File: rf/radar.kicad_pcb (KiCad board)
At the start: 4 copper layers, 52 x 68 mm, 136 parts, among them J101 Conn_01x02, J102 Conn_Coaxial, J103 Conn_01x04, J104 Conn_01x01, J105 Conn_01x01, J106 Conn_Coaxial, J107 Conn_01x02, J108 Conn_01x02, J801 Conn_01x02, T401 2450BL15B100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

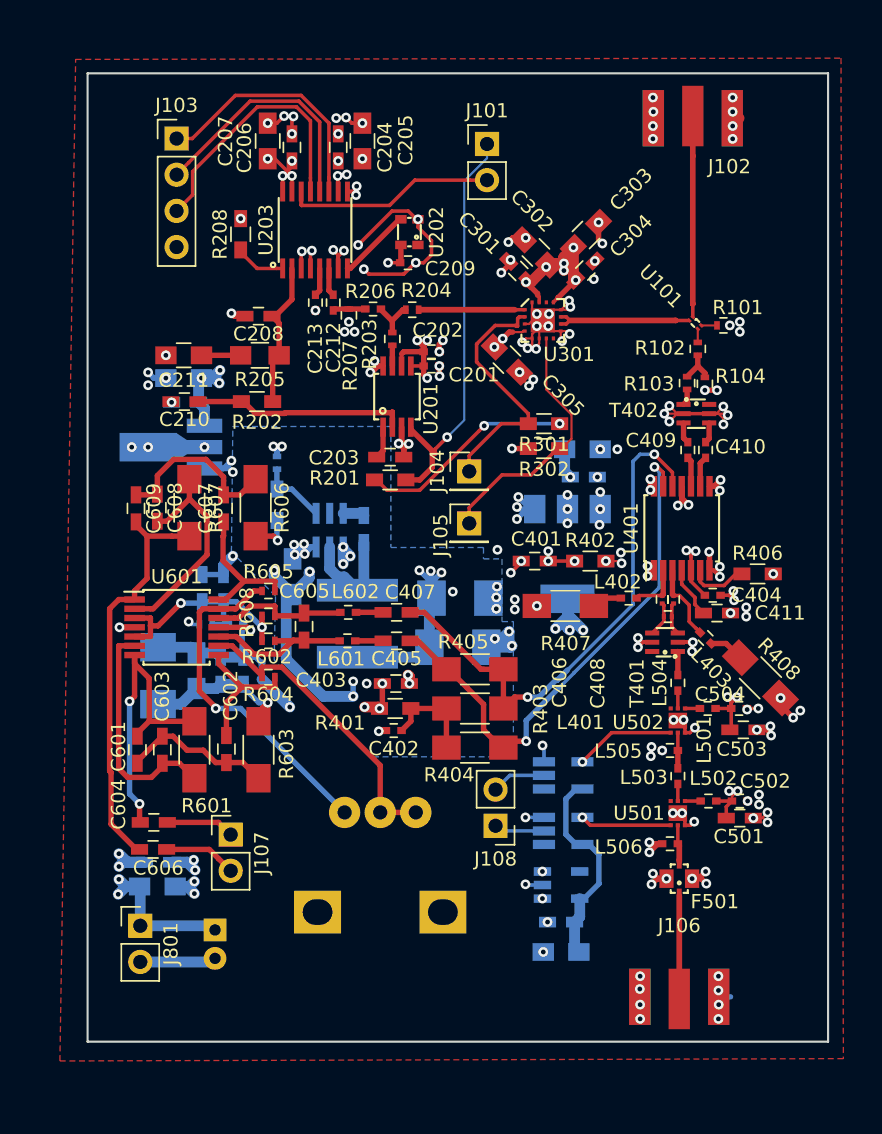
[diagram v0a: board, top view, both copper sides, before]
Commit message: Clean up PCB slightly
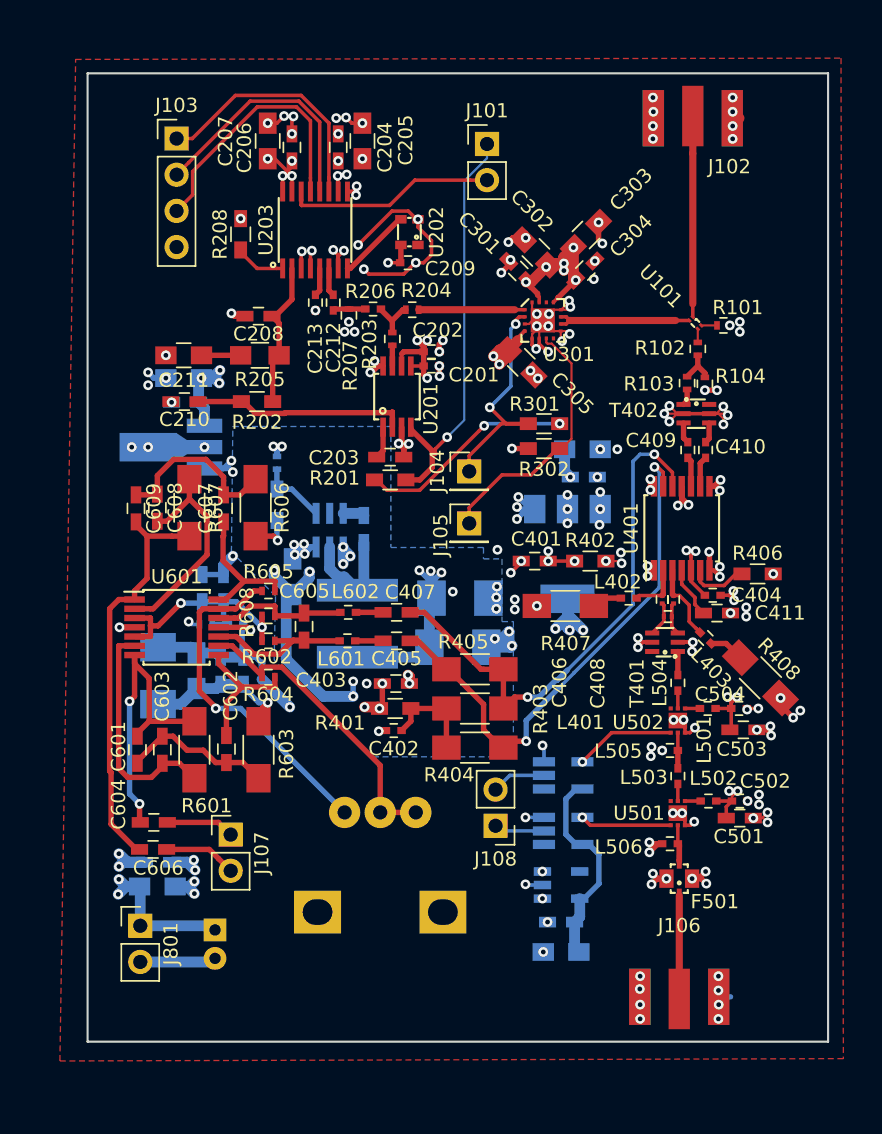
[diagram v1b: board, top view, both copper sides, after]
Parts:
- moved C305 1.02 mm to (130.5, 120.3)
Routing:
- net Net-(J102-Pad1): track 24.1 -> 14.1 mm
- net GND: track 831.8 -> 825.6 mm, vias 184 -> 182
- net /POWER_AMP/EN: track 17.8 -> 17.0 mm, vias 0 -> 2
- net /POWER_AMP/OUT: track 10.4 -> 9.83 mm

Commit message: Small fixes; update Gerber
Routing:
- net GND: track 825.6 -> 839.3 mm
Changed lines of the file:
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@@
     (thickness 1.6)
     (drawings 4)
-    (tracks 1740)
+    (tracks 1741)
     (zones 0)
     (modules 136)
@@
   )
   (setup
-    (last_trace_width 0.1524)
+    (last_trace_width 0.762)
     (user_trace_width 0.25)
     (user_trace_width 0.381)
@@
   (gr_line (start 152 100) (end 152 168) (layer Edge.Cuts) (width 0.15))
   (gr_line (start 100 100) (end 152 100) (layer Edge.Cuts) (width 0.15))
+  (segment (start 104.25 126.25) (end 104.25 124.75) (width 0.762) (layer B.Cu) (net 1))
+  (segment (start 104.25 124.75) (end 105.9 123.1) (width 0.762) (layer B.Cu) (net 1))
+  (segment (start 115.95 132.3) (end 115.95 130.9497) (width 0.762) (layer In2.Cu) (net 1))
+  (segment (start 115.95 130.9497) (end 115.95 130.45) (width 0.762) (layer In2.Cu) (net 1))
+  (segment (start 107.1877 130.9497) (end 115.95 130.9497) (width 0.762) (layer In2.Cu) (net 1))
+  (segment (start 104.25 126.25) (end 104.25 128.012) (width 0.762) (layer In2.Cu) (net 1))
+  (segment (start 104.25 128.012) (end 107.1877 130.9497) (width 0.762) (layer In2.Cu) (net 1))
+  (segment (start 104.25 126.25) (end 108.21 126.25) (width 0.762) (layer In2.Cu) (net 1))
+  (segment (start 103.1 126.25) (end 104.25 126.25) (width 0.762) (layer In2.Cu) (net 1))
   (segment (start 131.715 118.615) (end 131.715 119.0025) (width 0.25) (layer F.Cu) (net 1))
   (segment (start 128.4 129.7) (end 131 127.1) (width 0.762) (layer In1.Cu) (net 1))
@@
   (segment (start 117.95 133.262) (end 118.962 133.262) (width 0.762) (layer In2.Cu) (net 1))
   (segment (start 118.962 133.262) (end 119.35 132.874) (width 0.762) (layer In2.Cu) (net 1))
-  (segment (start 115.95 132.3) (end 115.95 130.45) (width 0.762) (layer In2.Cu) (net 1))
   (segment (start 116.912 133.262) (end 115.95 132.3) (width 0.762) (layer In2.Cu) (net 1))
   (segment (start 116.938 133.262) (end 116.912 133.262) (width 0.762) (layer In2.Cu) (net 1))
@@
   (segment (start 118.35 117.85) (end 118.05 118.15) (width 0.762) (layer In1.Cu) (net 1))
   (segment (start 115.75 112.45) (end 115.75 114.85) (width 0.762) (layer In1.Cu) (net 1))
-  (segment (start 108.21 126.25) (end 108.21 125.41) (width 0.762) (layer In1.Cu) (net 1))
-  (segment (start 108.21 125.41) (end 105.9 123.1) (width 0.762) (layer In1.Cu) (net 1))
-  (segment (start 103.1 126.25) (end 103.442899 125.907101) (width 0.762) (layer In1.Cu) (net 1))
-  (segment (start 103.442899 125.907101) (end 103.442899 125.557101) (width 0.762) (layer In1.Cu) (net 1))
-  (segment (start 103.442899 125.557101) (end 104.25 124.75) (width 0.762) (layer In1.Cu) (net 1))
-  (segment (start 104.25 126.25) (end 104.25 124.75) (width 0.762) (layer In1.Cu) (net 1))
-  (segment (start 104.25 124.75) (end 105.9 123.1) (width 0.762) (layer In1.Cu) (net 1))
   (segment (start 105.625 121.4) (end 106.275 120.75) (width 0.762) (layer In1.Cu) (net 1))
   (segment (start 106.275 120.75) (end 107.15 119.875) (width 0.762) (layer In1.Cu) (net 1))
@@
     (polygon
       (pts
-        (xy 121.3 124.8) (xy 121.3 129) (xy 121.3 133.3) (xy 127.8 133.3) (xy 127.8 134.1)
-        (xy 129.1 134.1) (xy 129.1 138.5) (xy 129.9 138.5) (xy 129.9 141.6) (xy 129.9 144.5)
-        (xy 129.9 148) (xy 119.9 148) (xy 113.1 141.2) (xy 113.2 136.7) (xy 110.1 133.6)
-        (xy 110.2 124.8)
+        (xy 121.3612 123.4567) (xy 121.3 133.3) (xy 127.8 133.3) (xy 127.8 134.1) (xy 129.1 134.1)
+        (xy 129.1 138.5) (xy 129.9 138.5) (xy 129.9 148) (xy 119.9 148) (xy 113.1 141.2)
+        (xy 113.2 136.7) (xy 110.1 133.6) (xy 110.15 129.2) (xy 101.5238 129.2352) (xy 101.6127 123.4186)
       )
     )
@@
         (xy 128.8 140.8) (xy 128.3 140.3) (xy 118 140.3) (xy 118 145) (xy 119 145)
         (xy 119 149) (xy 128 149) (xy 128 168) (xy 100 168) (xy 100 127.2)
-        (xy 128.3 127.2) (xy 128.3 126.7) (xy 100 126.7) (xy 100 100) (xy 152 100)
+        (xy 128.3 127.2) (xy 128.3 126.7) (xy 111.3028 126.7079) (xy 111.3028 125.1839) (xy 99.9998 125.1839)
+        (xy 100 100) (xy 152 100)
       )
     )

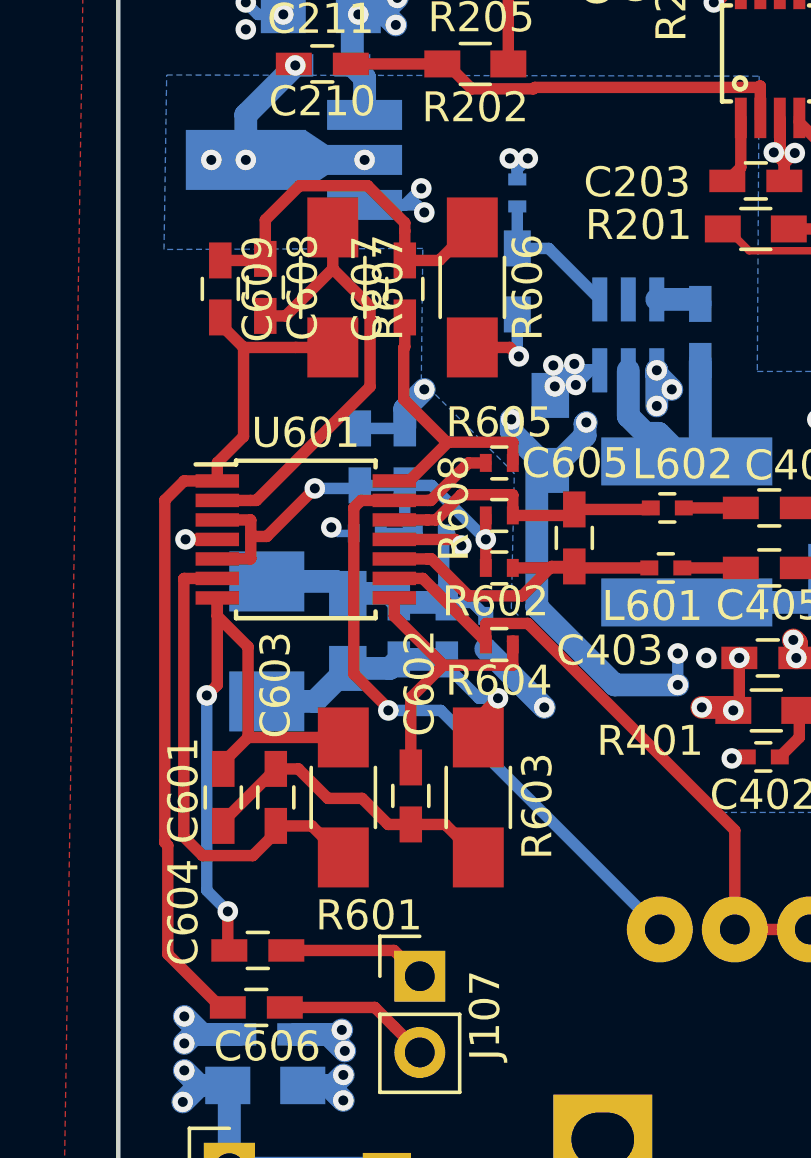
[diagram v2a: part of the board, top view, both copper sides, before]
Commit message: Convert high pass from MFB to Sallen-Key; forgot about low input impedance for high pass MFB
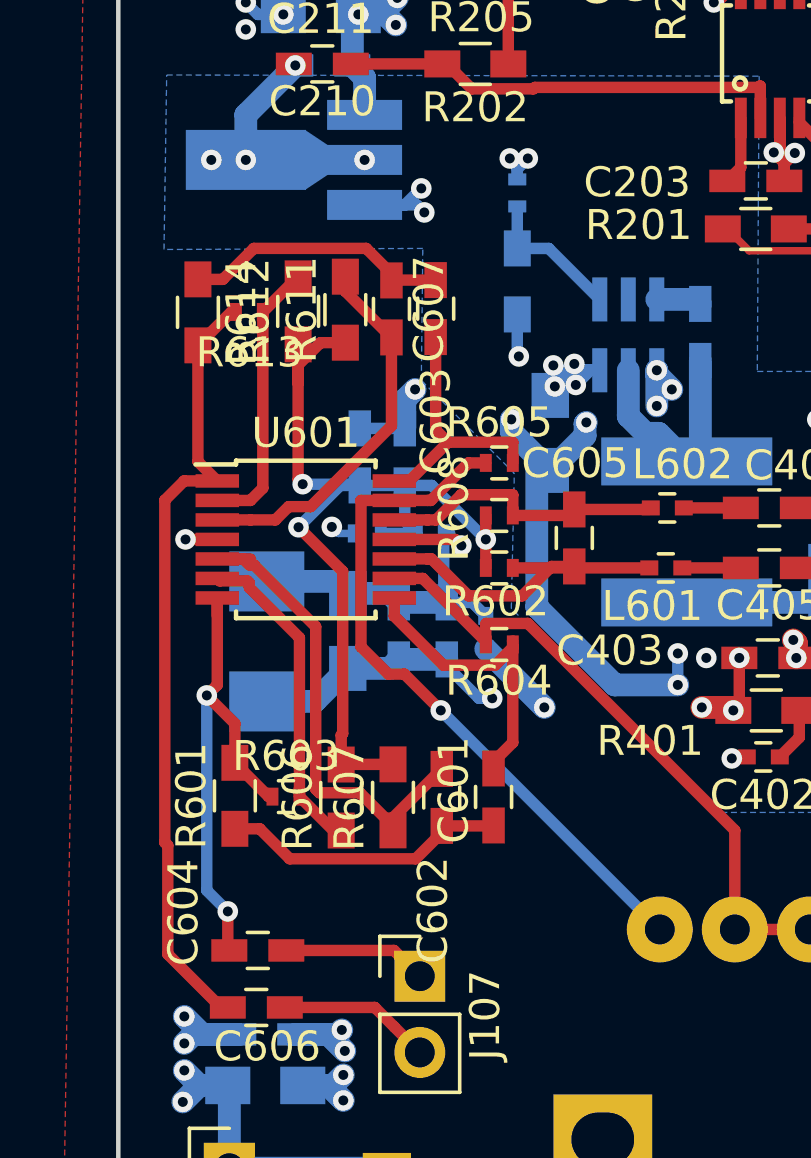
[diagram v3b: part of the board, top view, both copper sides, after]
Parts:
- removed C608: 8n5, Capacitors_SMD:C_0603_HandSoldering
- removed C609: 2n2, Capacitors_SMD:C_0603_HandSoldering
- added R611: 47k, Resistors_SMD:R_0603_HandSoldering, F.Cu at (107.6, 131.2)
- added R612: 47k, Resistors_SMD:R_0603_HandSoldering, F.Cu at (106.0, 131.3)
- added R613: 150k, Resistors_SMD:R_0402, F.Cu at (104.4, 131.3)
- added R614: 47k, Resistors_SMD:R_0603_HandSoldering, F.Cu at (102.7, 131.3)
- C601: value 2n2 -> 33p
- C602, C603, C607: value 8n5 -> 33p
- R601, R607: value 1k -> 47k; footprint Resistors_SMD:R_1206_HandSoldering -> Resistors_SMD:R_0603_HandSoldering
- R603: value 165 -> 150k; footprint Resistors_SMD:R_1206_HandSoldering -> Resistors_SMD:R_0402
- R606: value 165 -> 47k; footprint Resistors_SMD:R_1206_HandSoldering -> Resistors_SMD:R_0603_HandSoldering
- moved R606 17.6 mm to (107.4, 147.5), turned to 90 degrees
- moved C603 17.1 mm to (110.6, 131.2), turned to 90 degrees
- moved R607 17.1 mm to (109.2, 147.5), turned to 90 degrees
- moved C601 9.01 mm to (112.5, 147.5)
- moved R603 6.41 mm to (105.6, 147.5), turned to 0 degrees
- moved R601 3.61 mm to (103.9, 147.4), turned to 90 degrees
- moved C602 1.03 mm to (110.8, 147.5), turned to 90 degrees
- moved C607 0.80 mm to (109.1, 131.2), turned to 270 degrees
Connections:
- C602 pad 1: Net-(C602-Pad1) -> Net-(C601-Pad2)
- C602 pad 2: Net-(C601-Pad2) -> Net-(C602-Pad2)
- C603 pad 1: Net-(C601-Pad2) -> Net-(C603-Pad1)
- C604 pad 1: Net-(C601-Pad1) -> Net-(C604-Pad1)
- C607 pad 1: Net-(C607-Pad1) -> Net-(C603-Pad2)
- R601 pad 1: Net-(C601-Pad1) -> Net-(C601-Pad2)
- R601 pad 2: Net-(C603-Pad2) -> Net-(C604-Pad1)
- R603 pad 1: Net-(C601-Pad2) -> Net-(C604-Pad1)
- R603 pad 2: GND -> Net-(R603-Pad2)
- R604 pad 1: Net-(C602-Pad1) -> Net-(C601-Pad1)
- R605 pad 2: Net-(C607-Pad1) -> Net-(C603-Pad1)
- R606 pad 1: Net-(C607-Pad2) -> Net-(R603-Pad2)
- R606 pad 2: GND -> +6V
- R607 pad 1: Net-(C608-Pad2) -> Net-(C602-Pad2)
- R607 pad 2: Net-(C606-Pad1) -> +6V
- U601 pad 14: Net-(C607-Pad1) -> Net-(C603-Pad1)
- U601 pad 2: Net-(C608-Pad2) -> Net-(R612-Pad2)
- U601 pad 3: +6V -> Net-(C607-Pad2)
- U601 pad 5: +6V -> Net-(C602-Pad2)
- U601 pad 6: Net-(C603-Pad2) -> Net-(R603-Pad2)
- U601 pad 7: Net-(C601-Pad1) -> Net-(C604-Pad1)
- U601 pad 8: Net-(C602-Pad1) -> Net-(C601-Pad1)
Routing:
- net Net-(C604-Pad1): track 0.00 -> 17.2 mm, vias 0 -> 2
- net Net-(C602-Pad2): track 0.00 -> 16.0 mm
- net Net-(C608-Pad2): track 15.4 -> 0.00 mm
- net +6V: track 17.5 -> 31.8 mm, vias 2 -> 3
- net Net-(C601-Pad1): track 21.8 -> 9.99 mm, vias 2 -> 0
- net Net-(R603-Pad2): track 0.00 -> 10.8 mm
- net Net-(C607-Pad1): track 9.98 -> 0.00 mm
- net Net-(C602-Pad1): track 9.79 -> 0.00 mm
- net Net-(R612-Pad2): track 0.00 -> 9.20 mm
- net Net-(C603-Pad1): track 0.00 -> 8.89 mm
- net Net-(C603-Pad2): track 16.3 -> 8.93 mm
- net GND: track 839.3 -> 835.9 mm
- net Net-(C606-Pad1): track 29.0 -> 26.4 mm
- net Net-(C601-Pad2): track 10.6 -> 9.63 mm
- net Net-(R605-Pad1): track 24.3 -> 23.4 mm

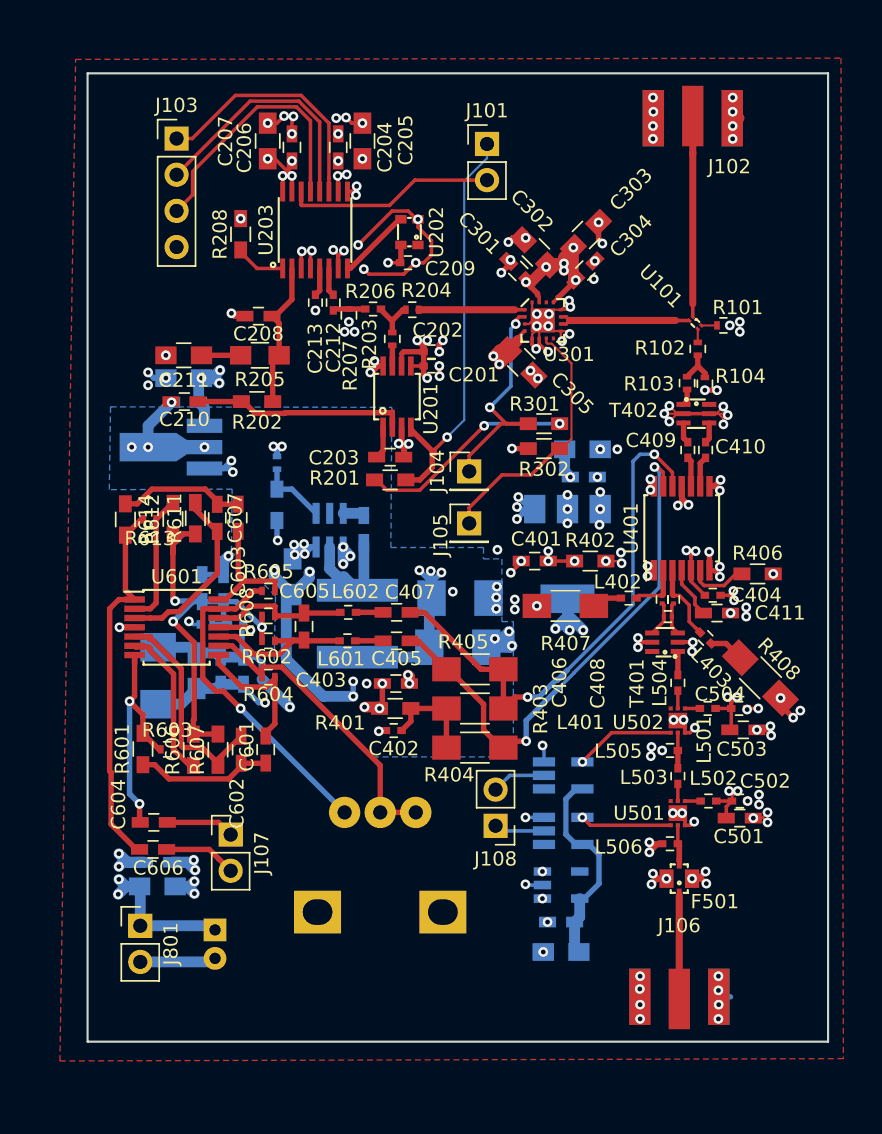
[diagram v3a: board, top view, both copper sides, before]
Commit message: Massage vias to improve planes and swap out connectors to get more ground lines
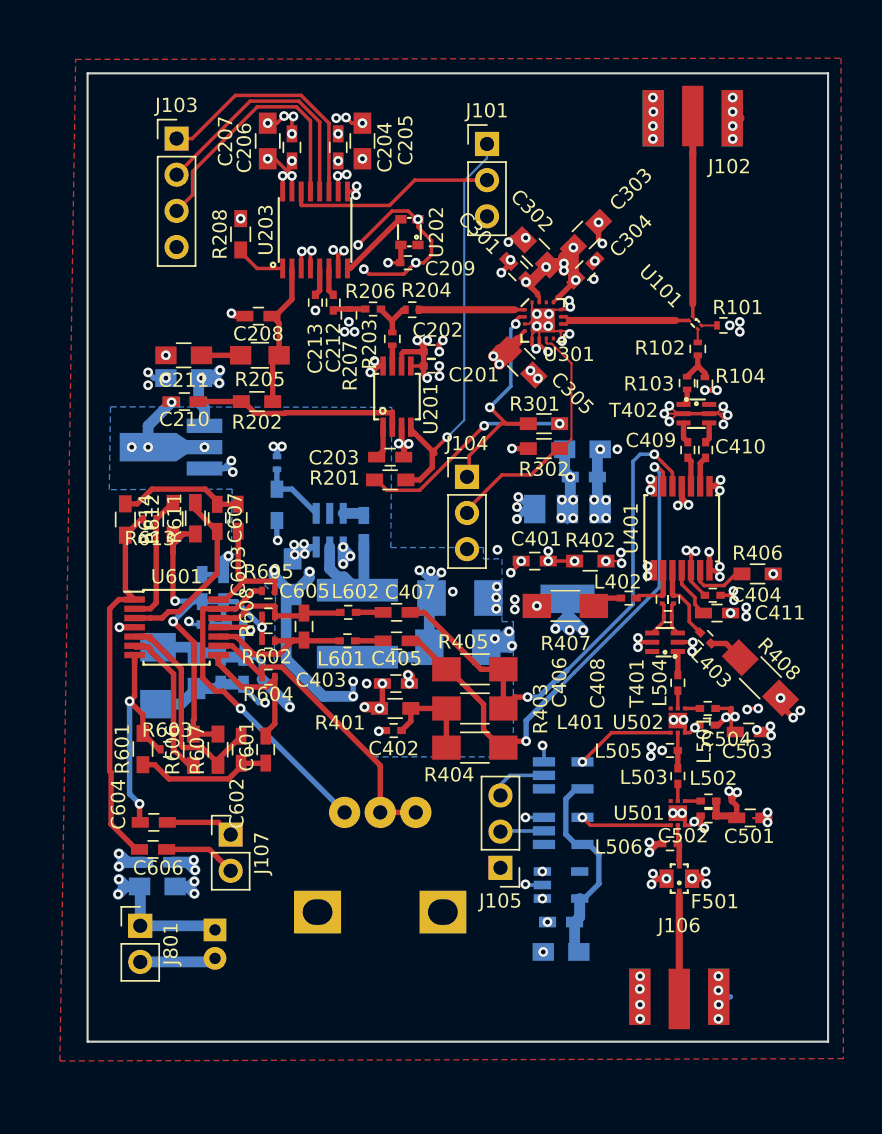
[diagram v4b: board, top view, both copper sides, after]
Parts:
- removed J108: Conn_01x02, Socket_Strips:Socket_Strip_Straight_1x02_Pitch2.54mm
- J101: value Conn_01x02 -> Conn_01x03; footprint Pin_Headers:Pin_Header_Straight_1x02_Pitch2.54mm -> Socket_Strips:Socket_Strip_Straight_1x03_Pitch2.54mm
- J104, J105: value Conn_01x01 -> Conn_01x03; footprint Socket_Strips:Socket_Strip_Straight_1x01_Pitch2.54mm -> Socket_Strips:Socket_Strip_Straight_1x03_Pitch2.54mm
- moved J105 24.3 mm to (129.0, 155.8), turned to 180 degrees
- moved C504 2.53 mm to (143.5, 145.8), turned to 180 degrees
- moved C502 2.44 mm to (143.6, 152.1), turned to 180 degrees
- moved C501 0.74 mm to (146.5, 152.3)
- moved J104 0.41 mm to (126.6, 128.3)
- moved C503 0.41 mm to (146.4, 146.3)
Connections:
- J105 pad 1: /POWER_AMP/PDET -> GND
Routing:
- net GND: track 835.9 -> 853.7 mm, vias 182 -> 180
- net Net-(C806-Pad1): track 70.6 -> 83.6 mm
- net +5V: track 95.3 -> 100.5 mm
- net +3V3: track 236.2 -> 239.7 mm
